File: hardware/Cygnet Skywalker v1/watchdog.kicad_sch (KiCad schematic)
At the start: 31 parts, among them J7 Conn_01x02, U14 TLV1704

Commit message: updated pcb progress
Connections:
- net VBUSP renamed WDT-VIN
- net WDT_WDI renamed PET DOG
- net ~{3v3_RESET} renamed DOG Bite
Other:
- note added: "I think this is to block DC current while still generating voltage?"
- moved on the sheet: JP6
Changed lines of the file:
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@@
 		)
 	)
+	(text "I think this is to block DC current while \nstill generating voltage?"
+		(exclude_from_sim no)
+		(at 83.566 109.474 0)
+		(effects
+			(font
+				(size 1.27 1.27)
+			)
+		)
+	)
 	(text "Pull-up on battery pack to Vbus"
 		(exclude_from_sim no)
@@
 	(text "WDT enabled\nwhen soldered"
 		(exclude_from_sim no)
-		(at 272.669 122.428 0)
+		(at 267.589 122.428 0)
 		(effects
 			(font
@@
 	(polyline
 		(pts
-			(xy 283.21 124.46) (xy 265.43 124.46)
+			(xy 278.765 124.46) (xy 260.35 124.46)
 		)
 		(stroke
@@
 	(wire
 		(pts
+			(xy 265.43 134.62) (xy 265.43 124.46)
+		)
+		(stroke
+			(width 0)
+			(type default)
+		)
+	)
+	(wire
+		(pts
 			(xy 137.16 114.3) (xy 137.16 115.57)
 		)
@@
 	(wire
 		(pts
-			(xy 247.65 116.84) (xy 270.51 116.84)
+			(xy 247.65 116.84) (xy 265.43 116.84)
 		)
 		(stroke
@@
 	(wire
 		(pts
-			(xy 111.76 111.76) (xy 113.03 111.76)
+			(xy 266.7 134.62) (xy 265.43 134.62)
 		)
 		(stroke
@@
 	(wire
 		(pts
-			(xy 30.48 36.83) (xy 30.48 53.34)
+			(xy 111.76 111.76) (xy 113.03 111.76)
 		)
 		(stroke
@@
 	(wire
 		(pts
-			(xy 193.04 139.7) (xy 191.77 139.7)
+			(xy 30.48 36.83) (xy 30.48 53.34)
 		)
 		(stroke
@@
 	(wire
 		(pts
-			(xy 231.14 68.58) (xy 231.14 86.36)
+			(xy 193.04 139.7) (xy 191.77 139.7)
 		)
 		(stroke
@@
 	(wire
 		(pts
-			(xy 204.47 134.62) (xy 204.47 127)
+			(xy 231.14 68.58) (xy 231.14 86.36)
 		)
 		(stroke
@@
 	(wire
 		(pts
-			(xy 90.17 60.96) (xy 204.47 60.96)
+			(xy 204.47 134.62) (xy 204.47 127)
 		)
 		(stroke
@@
 	(wire
 		(pts
-			(xy 270.51 124.46) (xy 270.51 127)
+			(xy 90.17 60.96) (xy 204.47 60.96)
 		)
 		(stroke
@@
 	(polyline
 		(pts
-			(xy 265.43 124.46) (xy 265.43 116.84)
+			(xy 260.35 124.46) (xy 260.35 117.475)
 		)
 		(stroke
@@
 	(polyline
 		(pts
-			(xy 265.43 116.84) (xy 283.21 115.57)
+			(xy 260.35 117.475) (xy 278.765 117.475)
 		)
 		(stroke
@@
 	(polyline
 		(pts
-			(xy 283.21 115.57) (xy 283.21 124.46)
+			(xy 278.765 117.475) (xy 278.765 124.46)
 		)
 		(stroke
@@
 		)
 	)
-	(global_label "VBUSP"
-		(shape bidirectional)
-		(at 30.48 36.83 90)
-		(fields_autoplaced yes)
-		(effects
-			(font
-				(size 1.27 1.27)
-			)
-			(justify left)
-		)
-		(property "Intersheetrefs" "${INTERSHEET_REFS}"
-			(at 30.48 26.5649 90)
-			(effects
-				(font
-					(size 1.27 1.27)
-				)
-				(justify left)
-				(hide yes)
-			)
-		)
-	)
-	(global_label "WDT_WDI"
+	(global_label "PET DOG"
 		(shape input)
 		(at 87.63 116.84 180)
@@
 			(font
 				(size 1.27 1.27)
-				(thickness 0.254)
-				(bold yes)
+				(thickness 0.1588)
 			)
 			(justify right)
 		)
 		(property "Intersheetrefs" "${INTERSHEET_REFS}"
-			(at 76.186 116.84 0)
+			(at 76.4201 116.84 0)
 			(effects
 				(font
@@
 		)
 	)
-	(global_label "~{3v3_RESET}"
+	(global_label "DOG Bite"
 		(shape output)
-		(at 270.51 127 270)
+		(at 266.7 134.62 0)
 		(fields_autoplaced yes)
 		(effects
@@
 				(size 1.27 1.27)
 			)
-			(justify right)
+			(justify left)
 		)
 		(property "Intersheetrefs" "${INTERSHEET_REFS}"
-			(at 270.51 140.0845 90)
+			(at 278.2124 134.62 0)
 			(effects
 				(font
 					(size 1.27 1.27)
 				)
-				(justify right)
+				(justify left)
 				(hide yes)
 			)
@@
 	(symbol
 		(lib_id "Jumper:SolderJumper_2_Open")
-		(at 270.51 120.65 270)
+		(at 265.43 120.65 270)
 		(unit 1)
 		(exclude_from_sim no)
@@
 		(dnp no)
 		(property "Reference" "JP6"
-			(at 267.716 120.904 0)
+			(at 262.636 120.904 0)
 			(effects
 				(font
@@
 		)
 		(property "Value" "SolderJumper_2_Open"
-			(at 284.48 120.65 90)
+			(at 279.4 120.65 90)
 			(effects
 				(font
@@
 		)
 		(property "Footprint" "Jumper:SolderJumper-2_P1.3mm_Open_RoundedPad1.0x1.5mm"
-			(at 270.51 120.65 0)
+			(at 265.43 120.65 0)
 			(effects
 				(font
@@
 		)
 		(property "Datasheet" "~"
-			(at 270.51 120.65 0)
+			(at 265.43 120.65 0)
 			(effects
 				(font
@@
 		)
 		(property "Description" ""
-			(at 270.51 120.65 0)
+			(at 265.43 120.65 0)
 			(effects
 				(font

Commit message: carried over changes to schematic made on max's branch
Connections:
- net WDT-VIN renamed +5V
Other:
- note added: "Watchdog based upon PROVES FC V5c's & Oresat's C3 Board"
- note removed: "I think this is to block DC current while still generating voltage?"
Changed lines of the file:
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@@
 		)
 	)
+	(text "Watchdog based upon PROVES FC V5c's & Oresat's C3 Board"
+		(exclude_from_sim no)
+		(at 70.358 166.878 0)
+		(effects
+			(font
+				(size 2.032 2.032)
+				(thickness 0.254)
+			)
+		)
+	)
 	(text "Do Not Consolidate the BOM on this Circuit"
 		(exclude_from_sim no)
@@
 		)
 	)
-	(text "I think this is to block DC current while \nstill generating voltage?"
-		(exclude_from_sim no)
-		(at 83.566 109.474 0)
-		(effects
-			(font
-				(size 1.27 1.27)
-			)
-		)
-	)
 	(text "Pull-up on battery pack to Vbus"
 		(exclude_from_sim no)
@@
 					(unit 1)
 				)
+			)
+		)
+	)
+	(symbol
+		(lib_id "power:+5V")
+		(at 30.48 36.83 0)
+		(unit 1)
+		(exclude_from_sim no)
+		(in_bom yes)
+		(on_board yes)
+		(dnp no)
+		(fields_autoplaced yes)
+		(property "Reference" "#PWR045"
+			(at 30.48 40.64 0)
+			(effects
+				(font
+					(size 1.27 1.27)
+				)
+				(hide yes)
+			)
+		)
+		(property "Value" "+5V"
+			(at 30.48 32.385 0)
+			(effects
+				(font
+					(size 1.27 1.27)
+				)
+			)
+		)
+		(property "Footprint" ""
+			(at 30.48 36.83 0)
+			(effects
+				(font
+					(size 1.27 1.27)
+				)
+				(hide yes)
+			)
+		)
+		(property "Datasheet" ""
+			(at 30.48 36.83 0)
+			(effects
+				(font
+					(size 1.27 1.27)
+				)
+				(hide yes)
+			)
+		)
+		(property "Description" "Power symbol creates a global label with name \"+5V\""
+			(at 30.48 36.83 0)
+			(effects
+				(font
+					(size 1.27 1.27)
+				)
+				(hide yes)
+			)
+		)
+		(pin "1"
+		)
+		(instances
+			(project "Cygnet Skywalker v1"
+				(path "/f674abc6-f811-4b69-a04b-9059ca6b6a44/f7e117b6-3b5d-4889-8e69-758ffca95a0e"
+					(reference "#PWR045")
+					(unit 1)
+				)

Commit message: brought over changes made on max branch
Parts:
- renumbered C27 to C34, C28 to C35, C29 to C36, C30 to C37, C31 to C38, D6 to D12, D7 to D13, R16 to R29, R17 to R30, R18 to R31, R19 to R32, R20 to R33, R21 to R34, R22 to R35, R28 to R36, R29 to R37, R30 to R38, R31 to R39, R32 to R40, R34 to R41, R36 to R42, R35 to R43, R33 to R44

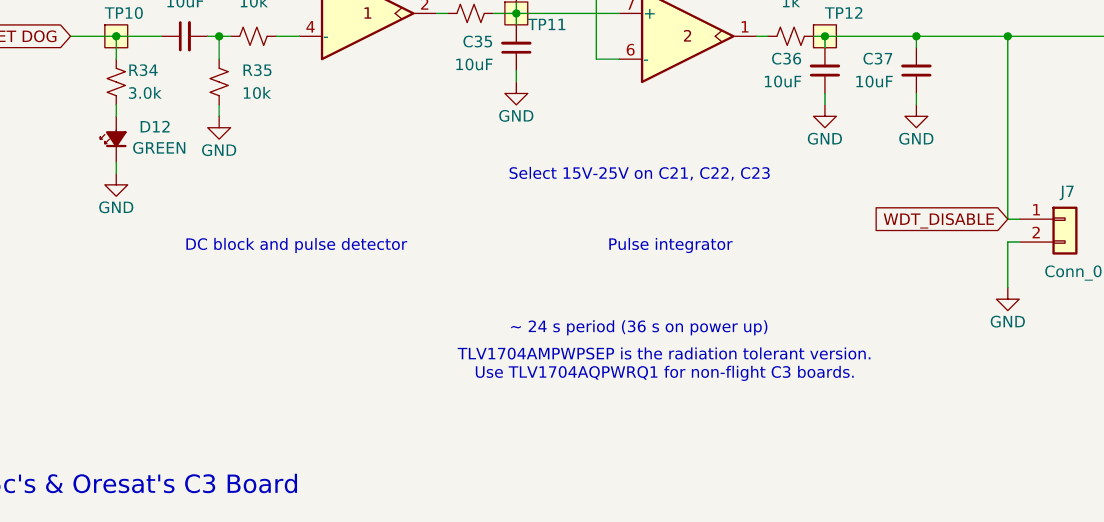
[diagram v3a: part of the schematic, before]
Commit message: updated schematic with mosfets
jfets no more for now. Also added footprints to some symbols.
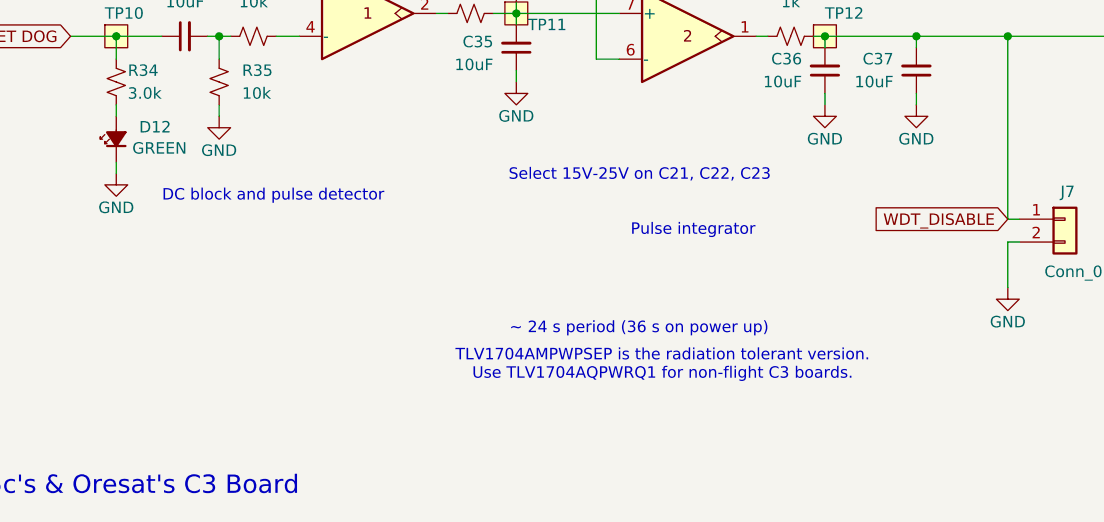
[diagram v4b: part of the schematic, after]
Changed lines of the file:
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@@
 	(text "TLV1704AMPWPSEP is the radiation tolerant version.\nUse TLV1704AQPWRQ1 for non-flight C3 boards."
 		(exclude_from_sim no)
-		(at 153.67 153.416 0)
+		(at 153.416 153.416 0)
 		(effects
 			(font
@@
 	(text "Pulse integrator"
 		(exclude_from_sim no)
-		(at 147.32 140.97 0)
+		(at 149.86 139.192 0)
 		(effects
 			(font
@@
 	(text "DC block and pulse detector"
 		(exclude_from_sim no)
-		(at 100.33 140.97 0)
+		(at 97.79 135.382 0)
 		(effects
 			(font

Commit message: final schematic used for layout
layout yay
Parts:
- renumbered C34 to C35, C35 to C36, C36 to C37, C37 to C38, C38 to C39, D12 to D11, D13 to D12, J7 to J10, JP6 to JP1, R29 to R24, R30 to R25, R31 to R26, R32 to R27, R33 to R28, R34 to R29, R35 to R30, R36 to R31, R37 to R32, R38 to R33, R39 to R34, R40 to R35, R44 to R36, R41 to R37, R43 to R38, R42 to R39, TP11 to TP10, TP12 to TP11, TP13 to TP12, TP9 to TP8, TP10 to TP9
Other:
- note added: "Watchdog based upon PROVES FC V5's & Oresat's C3 Board"
- note removed: "Watchdog based upon PROVES FC V5c's & Oresat's C3 Board"

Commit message: more footprints
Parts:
- C35, C36, C37, C38, C39: footprint Capacitor_SMD:C_0603_1608Metric -> Capacitor_SMD:C_0805_2012Metric
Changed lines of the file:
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@@
 			)
 		)
-		(property "Footprint" "Capacitor_SMD:C_0603_1608Metric"
+		(property "Footprint" "Capacitor_SMD:C_0805_2012Metric"
 			(at 100.33 116.84 0)
 			(effects
@@
 			)
 		)
-		(property "Footprint" "Capacitor_SMD:C_0603_1608Metric"
+		(property "Footprint" "Capacitor_SMD:C_0805_2012Metric"
 			(at 171.45 120.65 0)
 			(effects
@@
 			)
 		)
-		(property "Footprint" "Capacitor_SMD:C_0603_1608Metric"
+		(property "Footprint" "Capacitor_SMD:C_0805_2012Metric"
 			(at 137.16 118.11 0)
 			(effects
@@
 			)
 		)
-		(property "Footprint" "Capacitor_SMD:C_0603_1608Metric"
+		(property "Footprint" "Capacitor_SMD:C_0805_2012Metric"
 			(at 181.61 120.65 0)
 			(effects
@@
 			)
 		)
-		(property "Footprint" "Capacitor_SMD:C_0603_1608Metric"
+		(property "Footprint" "Capacitor_SMD:C_0805_2012Metric"
 			(at 236.22 90.17 0)
 			(effects

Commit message: carried over cygnet skywalker v1 from max-layout
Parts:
- C39: renamed from C35; footprint Capacitor_SMD:C_0805_2012Metric -> Capacitor_SMD:C_0603_1608Metric
- C40: renamed from C36; footprint Capacitor_SMD:C_0805_2012Metric -> Capacitor_SMD:C_0603_1608Metric
- C41: renamed from C37; footprint Capacitor_SMD:C_0805_2012Metric -> Capacitor_SMD:C_0603_1608Metric
- C42: renamed from C38; footprint Capacitor_SMD:C_0805_2012Metric -> Capacitor_SMD:C_0603_1608Metric
- C43: renamed from C39; footprint Capacitor_SMD:C_0805_2012Metric -> Capacitor_SMD:C_0603_1608Metric
- renumbered D11 to D12, D12 to D13, J10 to J12, R24 to R25, R25 to R26, R26 to R27, R27 to R28, R28 to R29, R29 to R30, R30 to R31, R31 to R32, R32 to R33, R33 to R34, R34 to R35, R35 to R36, R36 to R37, R37 to R38, R38 to R39, R39 to R40, TP8 to TP11, TP9 to TP12, TP10 to TP13, TP11 to TP14, TP12 to TP15, U14 to U15
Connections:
- net +5V renamed +3.3V
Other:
- note added: "Select 15V-25V on C36, C37, C38, C39"
- note removed: "Select 15V-25V on C21, C22, C23"

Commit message: push
finished footprint
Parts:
- renumbered C39 to C?, C41 to C?, C40 to C?, C42 to C?, C43 to C?, D13 to D?, D12 to D?, J12 to J?, JP1 to JP?, R30 to R?, R34 to R?, R28 to R?, R26 to R?, R31 to R?, R25 to R?, R39 to R?, R27 to R?, R29 to R?, R37 to R?, R36 to R?, R40 to R?, R38 to R?, R32 to R?, R35 to R?, R33 to R?, TP12 to TP?, TP11 to TP?, TP14 to TP?, TP15 to TP?, TP13 to TP?, U15 to U?
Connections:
- net +3.3V: no longer U?.3 (V+)
- net GND: no longer U?.12 (V-)
- net WDT_DISABLE: now also U?.4 (-); no longer U?.8 (-)
- net at C?.2, R?.2, R?.2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: now also U?.5 (+); no longer U?.7 (+)
- net at R?.1, R?.2: now also U?.4 (-); no longer U?.6 (-)
- net at C?.2, R?.1, R?.2: now also U?.4 (-); no longer U?.10 (-)
- net at D?.1, R?.1, R?.1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: now also U?.2, U?.5 (+); no longer U?.11 (+), U?.14
- net at JP?.1 (A): now also U?.2; no longer U?.13
- net at R?.1, R?.1: now also U?.5 (+); no longer U?.9 (+)
- net at R?.1: now also U?.2; no longer U?.1
